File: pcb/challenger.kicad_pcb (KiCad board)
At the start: 2 copper layers, 152.4 x 115.2 mm, 110 parts, among them SW1 SW_Push_45deg, SW10 SW_Push_45deg, SW11 SW_Push_45deg, SW12 SW_Push_45deg, SW13 SW_Push_45deg, SW14 SW_Push_45deg, SW15 SW_Push_45deg, SW16 SW_Push_45deg, SW17 SW_Push_45deg, SW18 SW_Push_45deg, SW19 SW_Push_45deg, SW2 SW_Push_45deg, SW20 SW_Push_45deg, SW21 SW_Push_45deg, SW22 SW_Push_45deg, SW23 SW_Push_45deg, SW24 SW_Push_45deg, SW25 SW_Push_45deg, SW26 SW_Push_45deg, SW27 SW_Push_45deg, SW28 SW_Push_45deg, SW29 SW_Push_45deg, SW3 SW_Push_45deg, SW30 SW_Push_45deg, SW31 SW_Push_45deg, SW32 SW_Push_45deg, SW33 SW_Push_45deg, SW34 SW_Push_45deg, SW35 SW_Push_45deg, SW36 SW_SPDT, SW37 SW_Push, SW4 SW_Push_45deg, SW5 SW_Push_45deg, SW6 SW_Push_45deg, SW7 SW_Push_45deg, SW8 SW_Push_45deg, SW9 SW_Push_45deg, U1 ProMicro

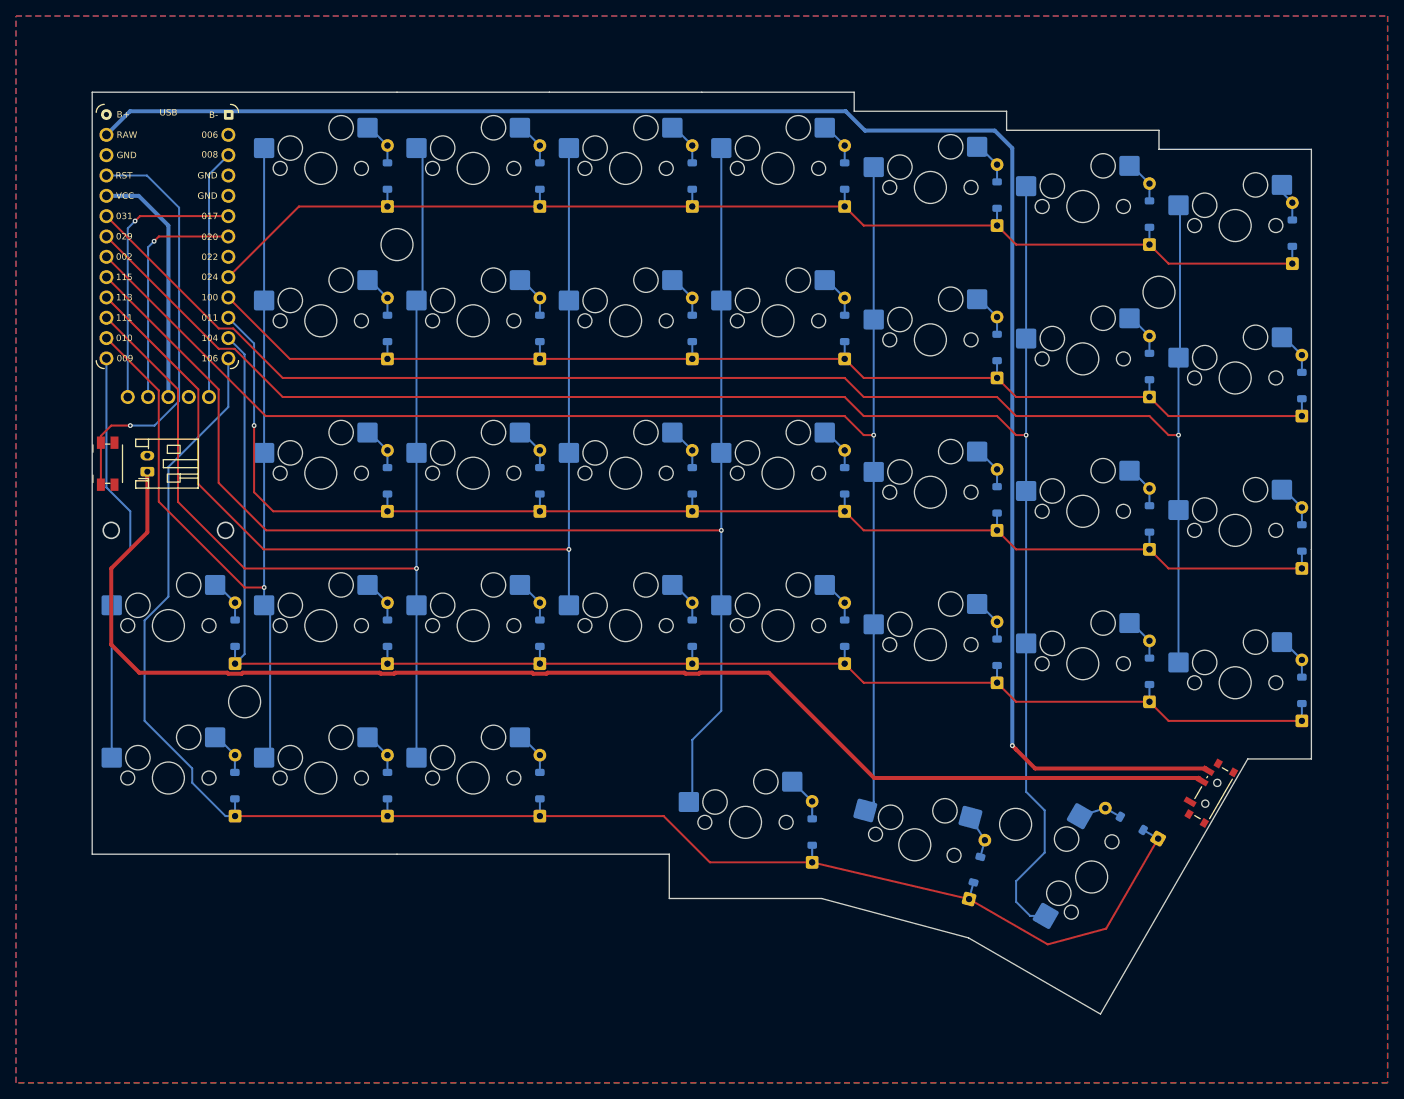
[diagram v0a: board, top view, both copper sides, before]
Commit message: feat: remove hybrid diode setup
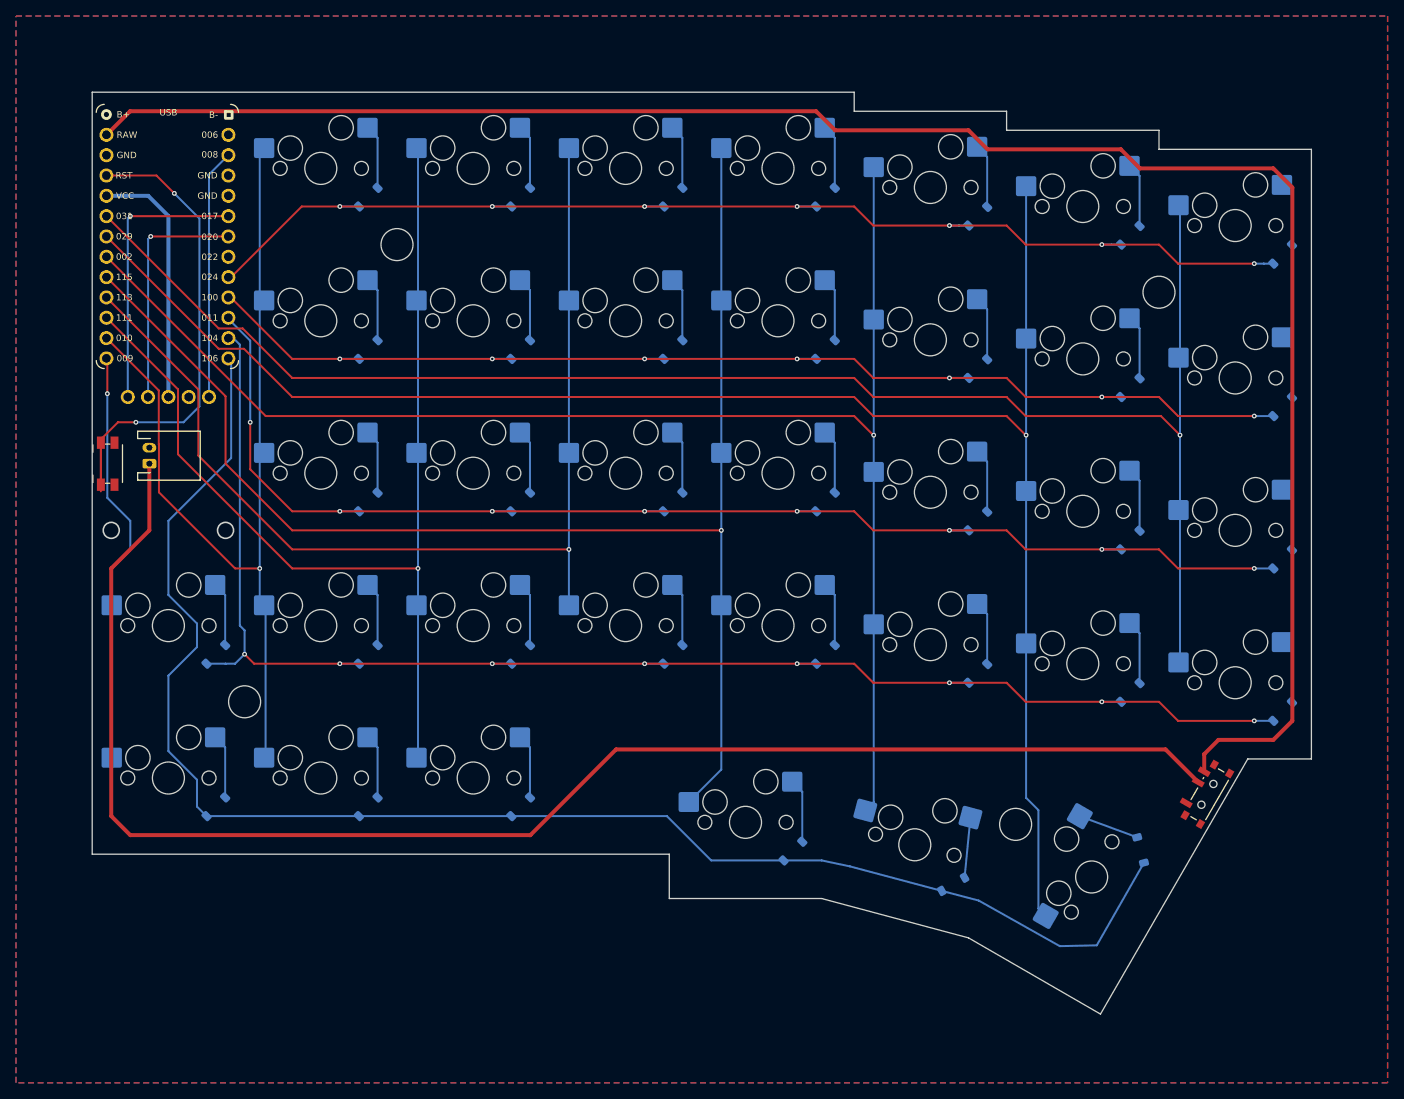
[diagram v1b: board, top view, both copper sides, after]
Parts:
- removed the D10 at (161.9, 54.8)
- removed the D12 at (181.0, 57.1)
- removed the D14 at (198.8, 59.5)
- removed the D16 at (85.7, 71.4)
- removed the D18 at (104.8, 71.4)
- removed the D2 at (85.7, 52.4)
- removed the D20 at (123.8, 71.4)
- removed the D22 at (142.9, 71.4)
- removed the D24 at (161.9, 73.8)
- removed the D26 at (181.0, 76.2)
- removed the D28 at (200.0, 78.6)
- removed the D30 at (85.7, 90.5)
- removed the D32 at (104.8, 90.5)
- removed the D34 at (123.8, 90.5)
- removed D36, D38, D40, D42, D44, D46, D48, D50, D52, D54, D56, D58, D60, D62, D64, D66, D68, D70: 1N4148, challenger:D_DO-35_SOD27_P7.62mm_Horizontal
- removed the D4 at (104.8, 52.4)
- removed the D6 at (123.8, 52.4)
- removed the D8 at (142.9, 52.4)
- BT1: footprint Connector_JST:JST_PH_S2B-PH-K_1x02_P2.00mm_Horizontal -> challenger:JST_PH_S2B-PH-K_1x02_P2.00mm_Horizontal
- SW36: footprint Button_Switch_SMD:SW_SPDT_PCM12 -> challenger:SW_SPDT_PCM12
- SW37: footprint Button_Switch_SMD:Panasonic_EVQPUJ_EVQPUA -> challenger:Panasonic_EVQPUJ_EVQPUA
- moved D33 3.58 mm to (135.2, 134.1), turned to 45 degrees
- moved D34 3.57 mm to (155.0, 137.9), turned to 30 degrees
- moved D10 3.57 mm to (120.3, 71.4), turned to 45 degrees
- moved D11 3.57 mm to (139.3, 71.4), turned to 45 degrees
- moved D12 3.57 mm to (158.4, 73.8), turned to 45 degrees
- moved D13 3.57 mm to (177.4, 76.2), turned to 45 degrees
- moved D14 3.57 mm to (196.5, 78.6), turned to 45 degrees
- moved D17 3.57 mm to (120.3, 90.5), turned to 45 degrees
- moved D18 3.57 mm to (139.3, 90.5), turned to 45 degrees
- moved D19 3.57 mm to (158.4, 92.9), turned to 45 degrees
- moved D20 3.57 mm to (177.4, 95.2), turned to 45 degrees
- moved D21 3.57 mm to (196.5, 97.6), turned to 45 degrees
- moved D25 3.57 mm to (120.3, 109.5), turned to 45 degrees
- moved D26 3.57 mm to (139.3, 109.5), turned to 45 degrees
- moved D27 3.57 mm to (158.4, 111.9), turned to 45 degrees
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- renumbered D19 to D10, D21 to D11, D23 to D12, D25 to D13, D27 to D14, D29 to D15, D31 to D16, D33 to D17, D35 to D18, D37 to D19, D3 to D2, D39 to D20, D41 to D21, D43 to D22, D45 to D23, D47 to D24, D49 to D25, D51 to D26, D53 to D27, D55 to D28, D57 to D29, D5 to D3, D59 to D30, D61 to D31, D63 to D32, D65 to D33, D67 to D34, D69 to D35, D7 to D4, D9 to D5, D11 to D6, D13 to D7, D15 to D8, D17 to D9
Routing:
- net Net-(BT1-+): track 167.3 -> 189.0 mm
- net B+: track 216.8 -> 235.0 mm, vias 1 -> 0
- net Row 4: track 207.0 -> 193.1 mm
- net RST: track 52.6 -> 63.1 mm, vias 1 -> 2
- net Row 2: track 173.3 -> 167.4 mm, vias 1 -> 8
- net Row 1: track 155.9 -> 151.0 mm, vias 0 -> 7
- net Column 6: track 221.6 -> 217.5 mm
- net Row 0: track 155.6 -> 151.5 mm, vias 0 -> 7
- net Column 2: track 136.8 -> 133.0 mm
- net Row 3: track 195.8 -> 192.3 mm, vias 0 -> 8
- net Net-(D7-A): track 5.19 -> 8.03 mm
- net Net-(D6-A): track 5.55 -> 8.03 mm
- net Net-(D5-A): track 5.55 -> 8.03 mm
- net Net-(D28-A): track 5.55 -> 8.03 mm
- net Net-(D20-A): track 5.55 -> 8.03 mm
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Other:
- outline, holes or cut-outs redrawn

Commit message: feat: update traces
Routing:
- net RST: track 63.1 -> 60.9 mm
- net Row 3: track 192.3 -> 193.8 mm
- net Column 1: track 115.3 -> 116.5 mm
- net Net-(BT1-+): track 189.0 -> 188.0 mm
- net Column 7: track 202.8 -> 203.6 mm

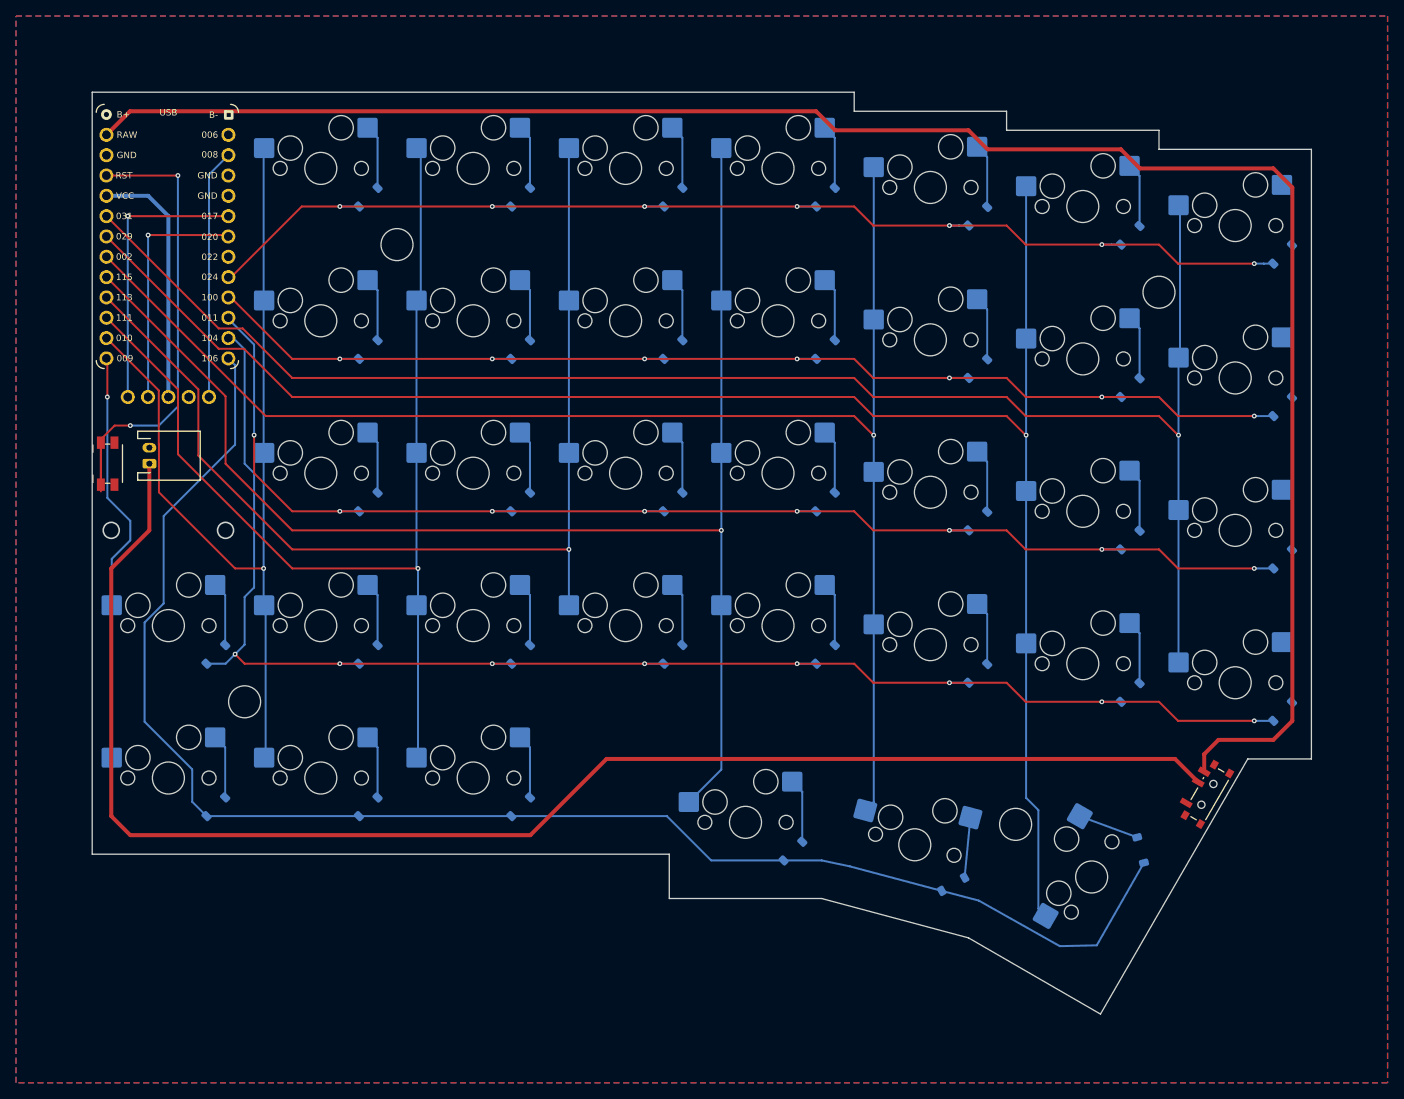
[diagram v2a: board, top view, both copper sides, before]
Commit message: feat: add switch and bottom plates and refine pcb
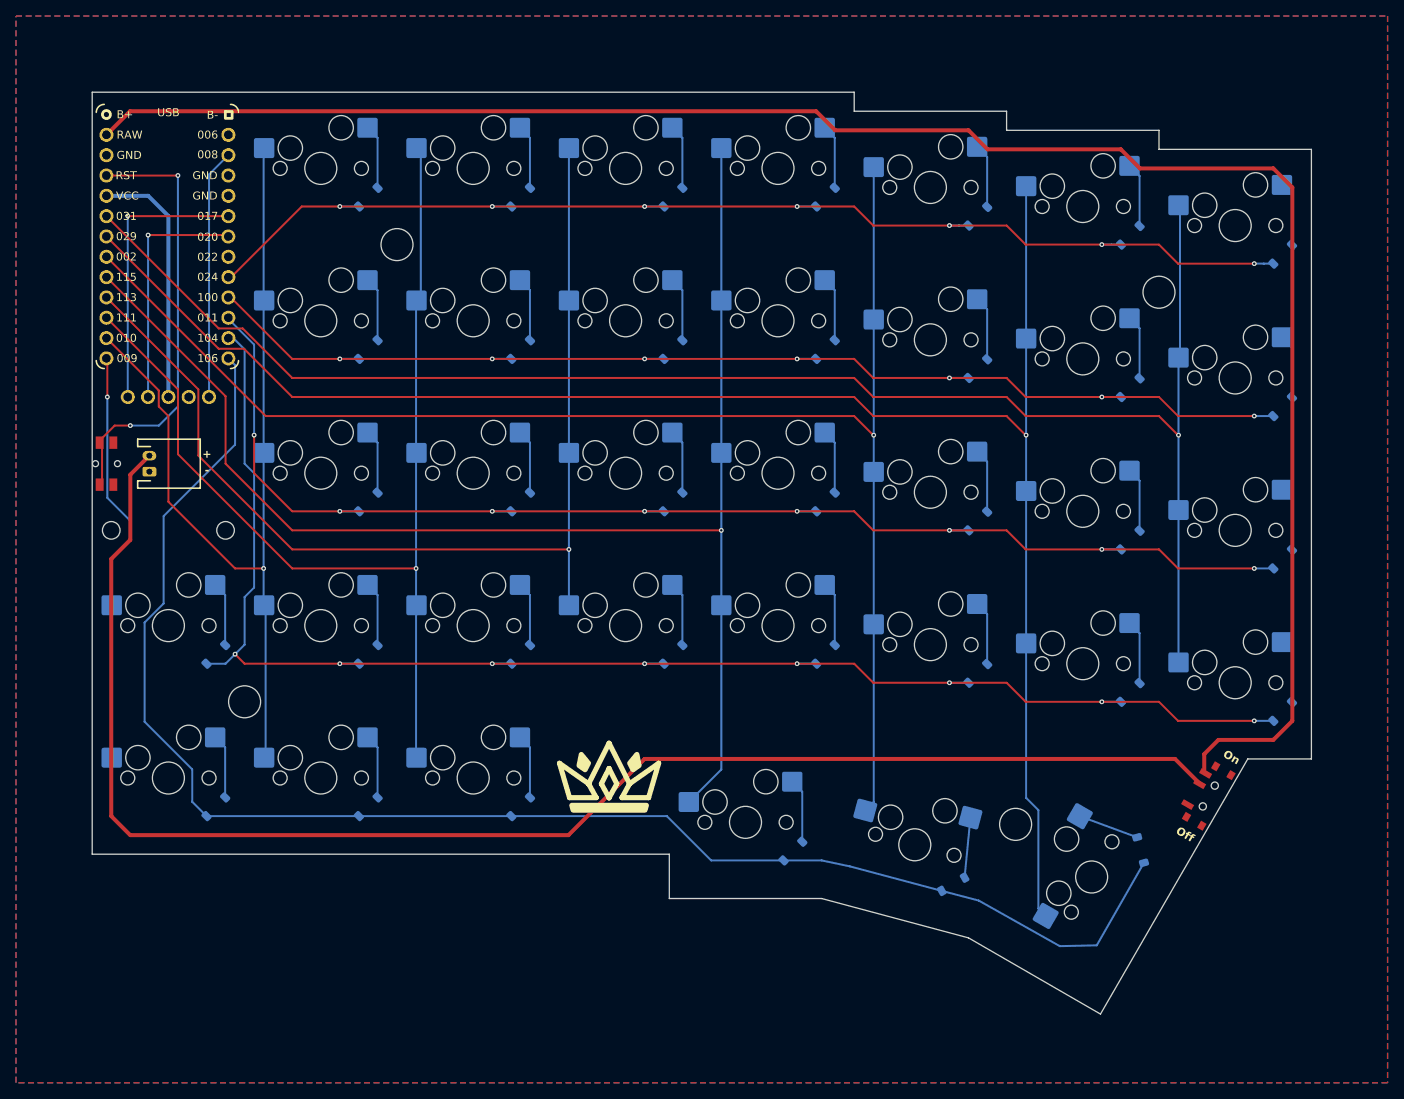
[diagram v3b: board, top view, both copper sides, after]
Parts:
- SW1, SW10, SW11, SW12, SW13, SW14, SW15, SW16, SW17, SW18, SW19, SW2, SW20, SW21, SW22, SW23, SW24, SW25, SW26, SW27, SW28, SW29, SW3, SW30, SW31, SW32, SW33, SW34, SW4, SW5, SW6, SW7, SW8, SW9: footprint challenger:SW_Hotswap_Kailh_MX_1.00u -> challenger:Hotswap_MX_1.00u
- SW35: footprint challenger:SW_Hotswap_Kailh_MX_1.50u -> challenger:Hotswap_MX_1.50u
- SW37: footprint challenger:Panasonic_EVQPUJ_EVQPUA -> challenger:Panasonic_EVQPUL_EVQPUC
- moved SW36 0.27 mm to (188.1, 125.9)
- moved SW37 0.15 mm to (50.6, 84.5)
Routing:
- net RST: track 60.9 -> 55.1 mm
- net Net-(BT1-+): track 188.0 -> 189.3 mm
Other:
- outline, holes or cut-outs redrawn
- board text added: "Challenger v0.1"
- board text added: "by @kevinpastor"

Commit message: feat: add logo and update font
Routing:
- net Row 4: track 193.0 -> 192.1 mm
